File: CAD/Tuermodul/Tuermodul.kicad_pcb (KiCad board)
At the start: 2 copper layers, 202.2 x 100.1 mm, 136 parts, among them J101 Conn_02x16_Counter_Clockwise, J201 Conn_02x20_Counter_Clockwise, J301 Conn_02x20_Counter_Clockwise, Q205 Q_NPN_CBE, Q206 Q_NPN_CBE, Q207 Q_NPN_CBE, Q208 Q_NPN_CBE, Q209 Q_PMOS_GDS, Q210 Q_PMOS_GDS, Q211 Q_PMOS_GDS, Q212 Q_PMOS_GDS, Q213 Q_NPN_CBE, Q214 Q_NPN_CBE, Q215 Q_NPN_CBE, Q216 Q_NPN_CBE, Q301 Q_NPN_CBE, SW301 SW_SPDT_MSM, SW302 SW_SPDT_MSM, SW303 SW_SPDT_MSM, SW304 SW_SPDT_MSM, U101 93LC46B, U102 74HC595, U103 FT4232H, U104 MCP1825S, Y101 12MHz

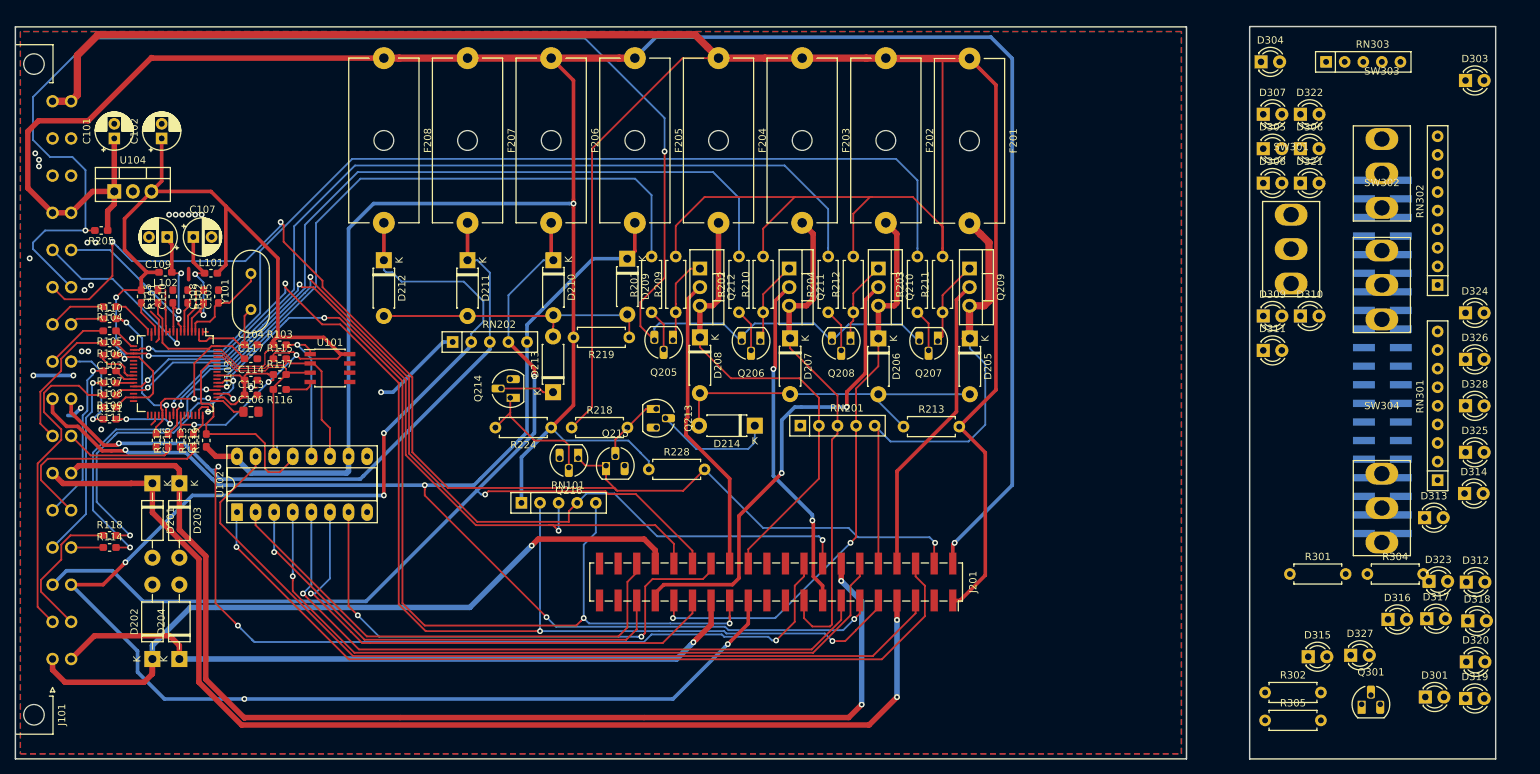
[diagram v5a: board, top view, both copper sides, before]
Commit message: -mod: Umbelegung Stecker zwischen Haupt und Frontplatine -add: 100n caps für MK Entprellung -mod: Routing Stecker -mod: Platzierung Front nach Vorgabe
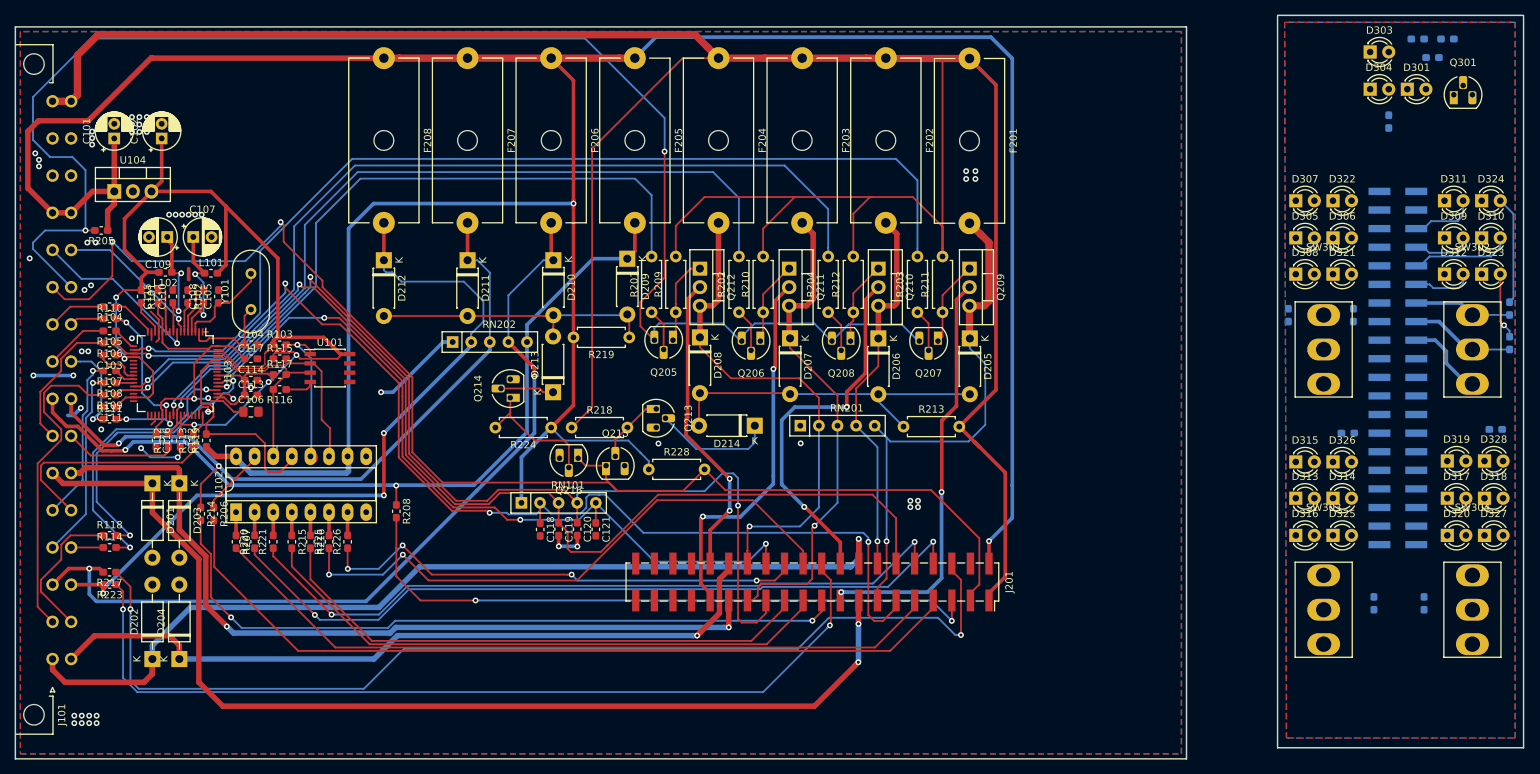
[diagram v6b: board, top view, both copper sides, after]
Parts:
- removed RN301: 8x2k7, Resistor_THT:R_Array_SIP9
- removed RN302: 8x10k, Resistor_THT:R_Array_SIP9
- removed RN303: 4x2k7, Resistor_THT:R_Array_SIP5
- added C118: 100n, Capacitor_SMD:C_0603_1608Metric_Pad1.05x0.95mm_HandSolder, F.Cu at (136.5, 113.1)
- added C119: 100n, Capacitor_SMD:C_0603_1608Metric_Pad1.05x0.95mm_HandSolder, F.Cu at (139.0, 113.1)
- added C120: 100n, Capacitor_SMD:C_0603_1608Metric_Pad1.05x0.95mm_HandSolder, F.Cu at (141.5, 113.1)
- added C121: 100n, Capacitor_SMD:C_0603_1608Metric_Pad1.05x0.95mm_HandSolder, F.Cu at (144.1, 113.1)
- added R206: 1k, Resistor_SMD:R_0603_1608Metric_Pad1.05x0.95mm_HandSolder, F.Cu at (91.9, 111.0)
- added R207: 1k, Resistor_SMD:R_0603_1608Metric_Pad1.05x0.95mm_HandSolder, F.Cu at (94.9, 114.8)
- added R208: 1k, Resistor_SMD:R_0603_1608Metric_Pad1.05x0.95mm_HandSolder, F.Cu at (116.8, 110.6)
- added R214: 1k, Resistor_SMD:R_0603_1608Metric_Pad1.05x0.95mm_HandSolder, F.Cu at (90.1, 111.0)
- added R215: 1k, Resistor_SMD:R_0603_1608Metric_Pad1.05x0.95mm_HandSolder, F.Cu at (102.5, 114.8)
- added R216: 1k, Resistor_SMD:R_0603_1608Metric_Pad1.05x0.95mm_HandSolder, F.Cu at (105.1, 114.8)
- added R217: 1k, Resistor_SMD:R_0603_1608Metric_Pad1.05x0.95mm_HandSolder, F.Cu at (77.6, 118.9)
- added R220: 1k, Resistor_SMD:R_0603_1608Metric_Pad1.05x0.95mm_HandSolder, F.Cu at (97.5, 114.8)
- added R221: 1k, Resistor_SMD:R_0603_1608Metric_Pad1.05x0.95mm_HandSolder, F.Cu at (100.0, 114.8)
- added R223: 1k, Resistor_SMD:R_0603_1608Metric_Pad1.05x0.95mm_HandSolder, F.Cu at (77.7, 120.6)
- added R225: 1k, Resistor_SMD:R_0603_1608Metric_Pad1.05x0.95mm_HandSolder, F.Cu at (107.6, 114.8)
- added R226: 1k, Resistor_SMD:R_0603_1608Metric_Pad1.05x0.95mm_HandSolder, F.Cu at (110.2, 114.8)
- added R303: 330R, Resistor_SMD:R_0603_1608Metric_Pad1.05x0.95mm_HandSolder, B.Cu at (256.4, 46.1)
- added R306: 4k7, Resistor_SMD:R_0603_1608Metric_Pad1.05x0.95mm_HandSolder, B.Cu at (238.7, 83.8)
- added R307: 4k7, Resistor_SMD:R_0603_1608Metric_Pad1.05x0.95mm_HandSolder, B.Cu at (268.9, 87.6)
- added R308: 4k7, Resistor_SMD:R_0603_1608Metric_Pad1.05x0.95mm_HandSolder, B.Cu at (268.9, 82.9)
- added R309: 4k7, Resistor_SMD:R_0603_1608Metric_Pad1.05x0.95mm_HandSolder, B.Cu at (250.4, 123.2)
- added R310: 4k7, Resistor_SMD:R_0603_1608Metric_Pad1.05x0.95mm_HandSolder, B.Cu at (246.8, 100.0)
- added R311: 4k7, Resistor_SMD:R_0603_1608Metric_Pad1.05x0.95mm_HandSolder, B.Cu at (257.2, 123.2)
- added R312: 4k7, Resistor_SMD:R_0603_1608Metric_Pad1.05x0.95mm_HandSolder, B.Cu at (267.0, 99.4)
- J201: value Conn_02x20_Counter_Clockwise -> Conn_02x20_Odd_Even
- R301, R302: footprint Resistor_THT:R_Axial_DIN0207_L6.3mm_D2.5mm_P7.62mm_Horizontal -> Resistor_SMD:R_0603_1608Metric_Pad1.05x0.95mm_HandSolder; moved to B.Cu
- R304: value 330R -> 1k; footprint Resistor_THT:R_Axial_DIN0207_L6.3mm_D2.5mm_P7.62mm_Horizontal -> Resistor_SMD:R_0603_1608Metric_Pad1.05x0.95mm_HandSolder; moved to B.Cu
- R305: value 1k -> 4k7; footprint Resistor_THT:R_Axial_DIN0207_L6.3mm_D2.5mm_P7.62mm_Horizontal -> Resistor_SMD:R_0603_1608Metric_Pad1.05x0.95mm_HandSolder; moved to B.Cu
- moved R302 89.7 mm to (258.4, 48.6)
- moved Q301 84.2 mm to (261.3, 53.7)
- moved D301 83.1 mm to (254.9, 53.0)
- moved R301 76.2 mm to (260.4, 46.1)
- moved R304 61.9 mm to (252.4, 57.4), turned to 270 degrees
- moved SW303 60.1 mm to (243.5, 124.1)
- moved R305 56.7 mm to (247.6, 83.8), turned to 270 degrees
- moved D323 42.6 mm to (265.1, 78.2)
- moved D312 42.2 mm to (260.0, 78.2)
- moved D319 32.5 mm to (260.4, 103.8)
- moved D311 32.1 mm to (260.0, 68.2)
- moved D310 27.0 mm to (265.1, 73.3)
- moved D309 27.0 mm to (260.0, 73.3)
- moved D315 26.7 mm to (239.7, 103.9)
- moved D327 24.5 mm to (265.5, 113.9)
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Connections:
- D305 pad 1: Net-(D305-Pad1) -> GNDA
- D306 pad 1: Net-(D306-Pad1) -> GNDA
- D307 pad 1: Net-(D307-Pad1) -> GNDA
- D309 pad 1: Net-(D309-Pad1) -> GNDA
- D310 pad 1: Net-(D310-Pad1) -> GNDA
- D311 pad 1: Net-(D311-Pad1) -> GNDA
- D313 pad 1: Net-(D313-Pad1) -> GNDA
- D314 pad 1: Net-(D314-Pad1) -> GNDA
- D315 pad 1: Net-(D315-Pad1) -> GNDA
- D317 pad 1: Net-(D317-Pad1) -> GNDA
- D318 pad 1: Net-(D318-Pad1) -> GNDA
- D319 pad 1: Net-(D319-Pad1) -> GNDA
- D321 pad 1: Net-(D321-Pad1) -> GNDA
- D321 pad 2: /Front/DoorA_Lock -> Net-(D321-Pad2)
- D322 pad 1: Net-(D322-Pad1) -> GNDA
- D322 pad 2: /Front/DoorA_12V -> Net-(D322-Pad2)
- D323 pad 1: Net-(D323-Pad1) -> GNDA
- D323 pad 2: /Front/DoorB_Lock -> Net-(D323-Pad2)
- D324 pad 1: Net-(D324-Pad1) -> GNDA
- D324 pad 2: /Front/DoorB_12V -> Net-(D324-Pad2)
- D325 pad 1: Net-(D325-Pad1) -> GNDA
- D325 pad 2: /Front/DoorC_Lock -> Net-(D325-Pad2)
- D326 pad 1: Net-(D326-Pad1) -> GNDA
- D326 pad 2: /Front/DoorC_12V -> Net-(D326-Pad2)
- D327 pad 1: Net-(D327-Pad1) -> GNDA
- D327 pad 2: /Front/DoorD_Lock -> Net-(D327-Pad2)
- D328 pad 1: Net-(D328-Pad1) -> GNDA
- D328 pad 2: /Front/DoorD_12V -> Net-(D328-Pad2)
- J201 pad 10: /Peripherie/DoorA_12V -> Net-(J201-Pad10)
- J201 pad 11: /DoorA_VCC -> /DoorA_MK
- J201 pad 12: /DC_Tx -> /DoorB_MK
- J201 pad 13: /DC_Rx -> /Peripherie/DoorA_12V
- J201 pad 14: /DoorC_Lock -> /Peripherie/DoorB_12V
- J201 pad 15: /Peripherie/DoorC_Auto -> /DoorA_Lock
- J201 pad 16: /DoorC_MK -> /DoorB_Lock
- J201 pad 17: /Peripherie/DoorC_12V -> /Peripherie/DoorA_Auto
- J201 pad 18: /DoorC_VCC -> /Peripherie/DoorB_Auto
- J201 pad 19: (no net) -> Net-(J201-Pad19)
- J201 pad 20: (no net) -> Net-(J201-Pad20)
- J201 pad 21: (no net) -> Net-(J201-Pad21)
- J201 pad 22: (no net) -> Net-(J201-Pad22)
- J201 pad 23: /DoorD_VCC -> Net-(J201-Pad23)
- J201 pad 24: /Peripherie/DoorD_12V -> Net-(J201-Pad24)
- J201 pad 25: /DoorD_MK -> /DoorC_MK
- J201 pad 26: /Peripherie/DoorD_Auto -> /DoorD_MK
- J201 pad 27: /DoorD_Lock -> /Peripherie/DoorC_12V
- J201 pad 28: /DD_Rx -> /Peripherie/DoorD_12V
- J201 pad 29: /DD_Tx -> /DoorC_Lock
- J201 pad 3: GND -> /Error
- J201 pad 30: /DoorB_VCC -> /DoorD_Lock
- J201 pad 31: /Peripherie/DoorB_12V -> /Peripherie/DoorC_Auto
- J201 pad 32: /DoorB_MK -> /Peripherie/DoorD_Auto
- J201 pad 33: /Peripherie/DoorB_Auto -> GND
- J201 pad 34: /DoorB_Lock -> GND
- J201 pad 35: /DB_Rx -> GND
- J201 pad 36: /DB_Tx -> GND
- J201 pad 37: (no net) -> GND
- J201 pad 38: (no net) -> GND
- J201 pad 39: (no net) -> GND
- J201 pad 4: /Error -> GND
- J201 pad 40: (no net) -> GND
- J201 pad 5: /DA_Tx -> Net-(J201-Pad5)
- J201 pad 6: /DA_Rx -> Net-(J201-Pad6)
- J201 pad 7: /DoorA_Lock -> Net-(J201-Pad7)
- J201 pad 8: /Peripherie/DoorA_Auto -> Net-(J201-Pad8)
- J201 pad 9: /DoorA_MK -> Net-(J201-Pad9)
- J301 pad 10: /Front/DoorA_12V -> /Front/DB_Rx
- J301 pad 11: /Front/DoorA_VCC -> /Front/DoorA_MK
- J301 pad 12: /Front/DC_Tx -> /Front/DoorB_MK
- J301 pad 13: /Front/DC_Rx -> /Front/DoorA_12V
- J301 pad 14: /Front/DoorC_Lock -> /Front/DoorB_12V
- J301 pad 15: /Front/DoorC_Auto -> /Front/DoorA_Lock
- J301 pad 16: /Front/DoorC_MK -> /Front/DoorB_Lock
- J301 pad 17: /Front/DoorC_12V -> /Front/DoorA_Auto
- J301 pad 18: /Front/DoorC_VCC -> /Front/DoorB_Auto
- J301 pad 19: (no net) -> /Front/DoorC_VCC
- J301 pad 20: (no net) -> /Front/DoorD_VCC
- J301 pad 21: (no net) -> /Front/DC_Tx
- J301 pad 22: (no net) -> /Front/DD_Tx
- J301 pad 23: /Front/DoorD_VCC -> /Front/DC_Rx
- J301 pad 24: /Front/DoorD_12V -> /Front/DD_Rx
- J301 pad 25: /Front/DoorD_MK -> /Front/DoorC_MK
- J301 pad 26: /Front/DoorD_Auto -> /Front/DoorD_MK
- J301 pad 27: /Front/DoorD_Lock -> /Front/DoorC_12V
- J301 pad 28: /Front/DD_Rx -> /Front/DoorD_12V
- J301 pad 29: /Front/DD_Tx -> /Front/DoorC_Lock
- J301 pad 3: GNDA -> /Front/Fuse_Error
- J301 pad 30: /Front/DoorB_VCC -> /Front/DoorD_Lock
- J301 pad 31: /Front/DoorB_12V -> /Front/DoorC_Auto
- J301 pad 32: /Front/DoorB_MK -> /Front/DoorD_Auto
- J301 pad 33: /Front/DoorB_Auto -> GNDA
- J301 pad 34: /Front/DoorB_Lock -> GNDA
- J301 pad 35: /Front/DB_Rx -> GNDA
- J301 pad 36: /Front/DB_Tx -> GNDA
- J301 pad 37: (no net) -> GNDA
- J301 pad 38: (no net) -> GNDA
- J301 pad 39: (no net) -> GNDA
- J301 pad 4: /Front/Fuse_Error -> GNDA
- J301 pad 40: (no net) -> GNDA
- J301 pad 5: /Front/DA_Tx -> /Front/DoorA_VCC
- J301 pad 6: /Front/DA_Rx -> /Front/DoorB_VCC
- J301 pad 7: /Front/DoorA_Lock -> /Front/DA_Tx
- J301 pad 8: /Front/DoorA_Auto -> /Front/DB_Tx
- J301 pad 9: /Front/DoorA_MK -> /Front/DA_Rx
- R304 pad 1: +5P -> +12P
- R304 pad 2: Net-(D303-Pad2) -> Net-(D304-Pad2)
- R305 pad 1: +12P -> Net-(D321-Pad2)
- R305 pad 2: Net-(D304-Pad2) -> /Front/DoorA_Lock
- U101 pad 6: (no net) -> Net-(U101-Pad6)
- U101 pad 7: (no net) -> Net-(U101-Pad7)
- U102 pad 9: (no net) -> Net-(U102-Pad9)
- U103 pad 21: (no net) -> Net-(U103-Pad21)
- U103 pad 22: (no net) -> Net-(U103-Pad22)
- U103 pad 23: (no net) -> Net-(U103-Pad23)
- U103 pad 24: (no net) -> Net-(U103-Pad24)
- U103 pad 30: (no net) -> Net-(U103-Pad30)
- U103 pad 32: (no net) -> Net-(U103-Pad32)
- U103 pad 33: (no net) -> Net-(U103-Pad33)
- U103 pad 34: (no net) -> Net-(U103-Pad34)
- U103 pad 36: (no net) -> Net-(U103-Pad36)
- U103 pad 43: (no net) -> Net-(U103-Pad43)
- U103 pad 44: (no net) -> Net-(U103-Pad44)
- U103 pad 45: (no net) -> Net-(U103-Pad45)
- U103 pad 46: (no net) -> Net-(U103-Pad46)
- U103 pad 55: (no net) -> Net-(U103-Pad55)
- U103 pad 57: (no net) -> Net-(U103-Pad57)
- U103 pad 58: (no net) -> Net-(U103-Pad58)
- U103 pad 59: (no net) -> Net-(U103-Pad59)
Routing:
- net Net-(J201-Pad6): track 0.00 -> 144.8 mm, vias 0 -> 2
- net Net-(J201-Pad20): track 0.00 -> 123.3 mm, vias 0 -> 2
- net Net-(J201-Pad7): track 0.00 -> 113.9 mm
- net /DA_Rx: track 115.4 -> 3.17 mm, vias 1 -> 0
- net /DA_Tx: track 117.8 -> 9.30 mm
- net /DoorD_VCC: track 209.8 -> 103.8 mm, vias 5 -> 3
- net /DoorC_VCC: track 202.4 -> 97.3 mm, vias 4 -> 2
- net Net-(J201-Pad8): track 0.00 -> 104.7 mm, vias 0 -> 2
- net Net-(J201-Pad9): track 0.00 -> 101.6 mm
- net Net-(J201-Pad19): track 0.00 -> 99.7 mm, vias 0 -> 2
- net Net-(J201-Pad10): track 0.00 -> 99.1 mm, vias 0 -> 2
- net /DC_Tx: track 100.2 -> 3.17 mm, vias 1 -> 0
- net /DC_Rx: track 92.6 -> 3.17 mm, vias 1 -> 0
- net Net-(J201-Pad5): track 0.00 -> 89.3 mm, vias 0 -> 2
- net Net-(J201-Pad22): track 0.00 -> 80.1 mm, vias 0 -> 2
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- added copper zone on B.Cu, net GNDA
- added copper zone on F.Cu, net GNDA
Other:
- board size 202.2 x 100.1 mm -> 206.1 x 101.6 mm

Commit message: -mod: layout update from 10.03.19
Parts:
- added REF**: MountingHole_2.5mm, MountingHole:MountingHole_2.5mm, F.Cu at (253.7, 60.6)
- added REF**: MountingHole_2.5mm, MountingHole:MountingHole_2.5mm, F.Cu at (253.7, 136.8)
- moved R305 9.67 mm to (238.7, 87.6)
- moved R304 5.51 mm to (246.9, 56.8), turned to 0 degrees
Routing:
- net /Front/DoorD_12V: track 0.00 -> 39.6 mm, vias 0 -> 3
- net /Front/DoorD_Lock: track 0.00 -> 37.0 mm, vias 0 -> 1
- net /Front/DoorC_Lock: track 0.00 -> 36.4 mm, vias 0 -> 1
- net /Front/DoorC_12V: track 0.00 -> 33.0 mm, vias 0 -> 1
- net /Front/DoorC_Auto: track 0.00 -> 32.0 mm, vias 0 -> 1
- net /Front/DoorD_Auto: track 0.00 -> 29.7 mm, vias 0 -> 1
- net Net-(D322-Pad2): track 0.00 -> 28.1 mm
- net +5P: track 0.00 -> 26.8 mm, vias 0 -> 2
- net /Front/DC_Tx: track 0.00 -> 25.5 mm, vias 0 -> 1
- net /Front/DD_Rx: track 0.00 -> 25.5 mm, vias 0 -> 1
- net /Front/DoorC_MK: track 0.00 -> 24.7 mm, vias 0 -> 1
- net /Front/DD_Tx: track 0.00 -> 22.7 mm, vias 0 -> 2
- net /Front/DoorD_MK: track 0.00 -> 21.6 mm, vias 0 -> 1
- net /Front/Fuse_Error: track 0.00 -> 21.6 mm
- net /Front/DC_Rx: track 0.00 -> 18.7 mm, vias 0 -> 1
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
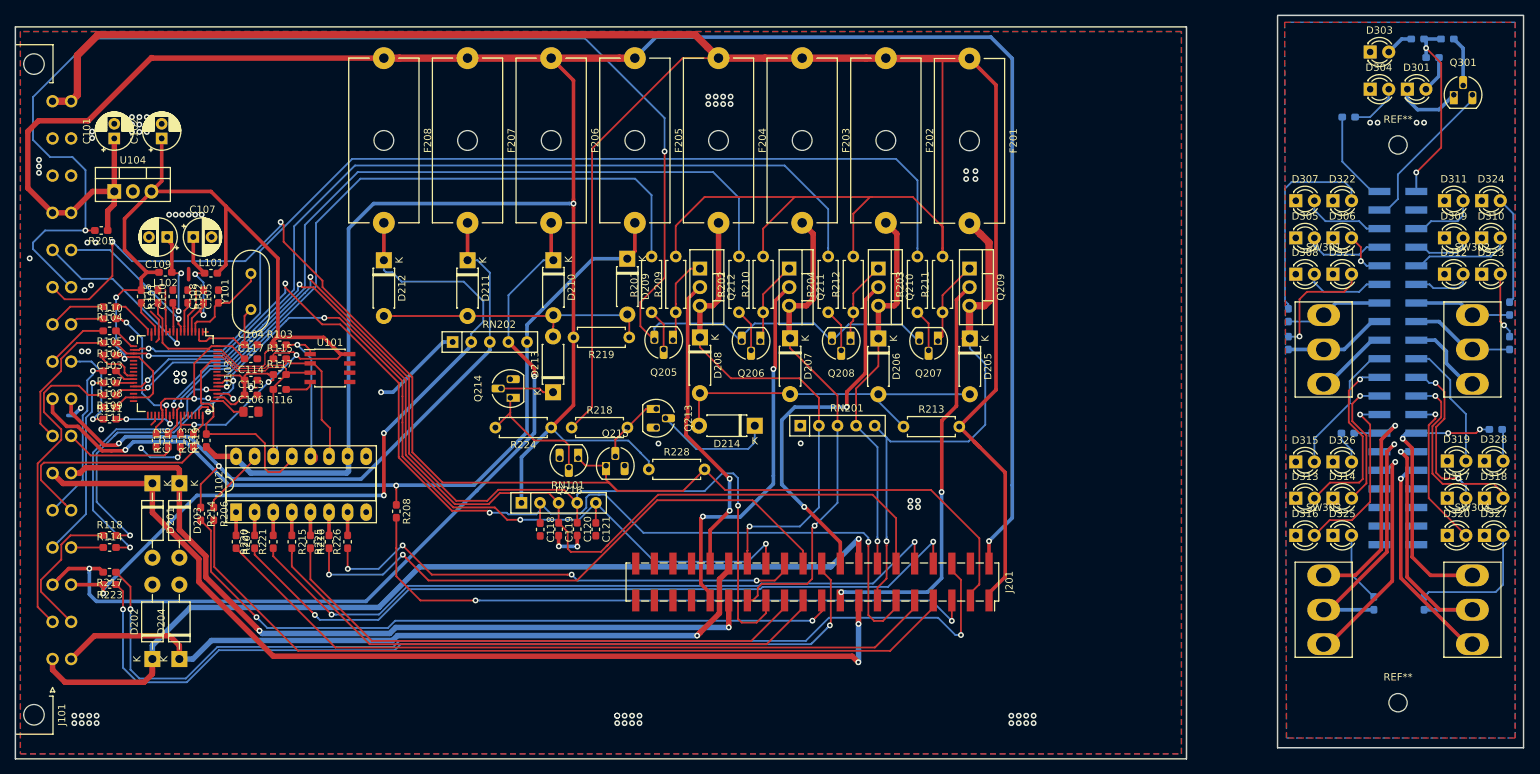
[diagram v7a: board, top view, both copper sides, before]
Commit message: -mod: Änderungen aus Review in Schaltplan und Layout
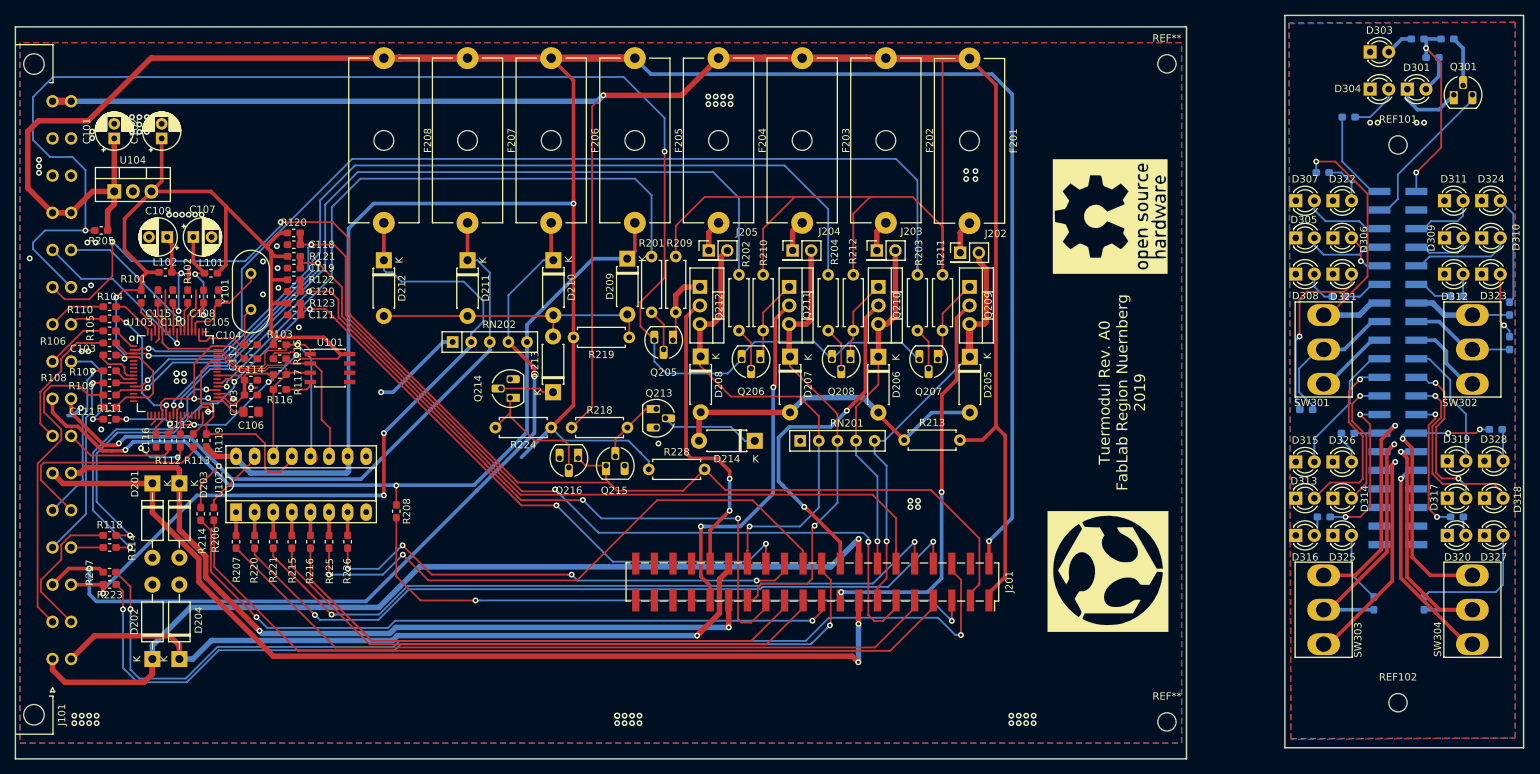
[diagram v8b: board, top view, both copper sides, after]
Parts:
- removed RN101: 2k7, Resistor_THT:R_Array_SIP5
- added G101: LOGO, FLN_logo:fln_logo, F.Cu at (214.0, 118.9)
- added G102: LOGO, OSH_logo:OSH_logo, F.Cu at (214.3, 70.4)
- added J202: Conn_02x01, Connector_PinHeader_2.54mm:PinHeader_2x01_P2.54mm_Vertical, F.Cu at (193.9, 75.3)
- added J203: Conn_02x01, Connector_PinHeader_2.54mm:PinHeader_2x01_P2.54mm_Vertical, F.Cu at (182.5, 75.0)
- added J204: Conn_02x01, Connector_PinHeader_2.54mm:PinHeader_2x01_P2.54mm_Vertical, F.Cu at (171.0, 75.0)
- added J205: Conn_02x01, Connector_PinHeader_2.54mm:PinHeader_2x01_P2.54mm_Vertical, F.Cu at (159.5, 75.0)
- added R120: 1k, Resistor_SMD:R_0603_1608Metric_Pad1.05x0.95mm_HandSolder, F.Cu at (102.8, 72.6)
- added R121: 1k, Resistor_SMD:R_0603_1608Metric_Pad1.05x0.95mm_HandSolder, F.Cu at (102.8, 75.8)
- added R122: 1k, Resistor_SMD:R_0603_1608Metric_Pad1.05x0.95mm_HandSolder, F.Cu at (102.8, 79.0)
- added R123: 1k, Resistor_SMD:R_0603_1608Metric_Pad1.05x0.95mm_HandSolder, F.Cu at (102.8, 82.2)
- added R313: 470R, Resistor_SMD:R_0603_1608Metric_Pad1.05x0.95mm_HandSolder, B.Cu at (245.6, 81.3)
- added R314: 470R, Resistor_SMD:R_0603_1608Metric_Pad1.05x0.95mm_HandSolder, B.Cu at (261.7, 81.2)
- added R315: 470R, Resistor_SMD:R_0603_1608Metric_Pad1.05x0.95mm_HandSolder, B.Cu at (243.5, 111.4)
- added R316: 470R, Resistor_SMD:R_0603_1608Metric_Pad1.05x0.95mm_HandSolder, B.Cu at (261.7, 111.4)
- added REF**: MountingHole_2.5mm, MountingHole:MountingHole_2.5mm, F.Cu at (222.1, 49.5)
- added REF**: MountingHole_2.5mm, MountingHole:MountingHole_2.5mm, F.Cu at (222.1, 139.4)
- R106, R109, R112, R118: value 33R -> 100R
- moved C118 51.4 mm to (102.8, 74.2), turned to 180 degrees
- moved C119 50.8 mm to (102.8, 77.4), turned to 180 degrees
- moved C121 50.5 mm to (102.9, 83.8), turned to 180 degrees
- moved C120 50.5 mm to (102.8, 80.6), turned to 180 degrees
- moved R306 20.0 mm to (243.4, 64.3), turned to 180 degrees
- moved R305 9.43 mm to (241.1, 96.8), turned to 0 degrees
- moved D208 2.61 mm to (158.4, 89.5)
- moved D205 2.50 mm to (195.2, 89.5)
- moved D206 2.50 mm to (182.7, 89.5)
- moved D207 2.50 mm to (170.6, 89.5)
- moved Q206 2.50 mm to (166.5, 89.9)
- moved Q207 2.50 mm to (190.8, 89.9)
- moved Q208 2.50 mm to (178.9, 89.9)
- moved Q209 2.50 mm to (195.1, 80.0)
- moved Q210 2.50 mm to (182.7, 80.0)
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- renumbered REF** to REF101, REF** to REF102
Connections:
- D308 pad 2: /Front/DoorA_MK -> Net-(D308-Pad2)
- D312 pad 2: /Front/DoorB_MK -> Net-(D312-Pad2)
- D316 pad 2: /Front/DoorC_MK -> Net-(D316-Pad2)
- D320 pad 2: /Front/DoorD_MK -> Net-(D320-Pad2)
- F201 pad 2: /Peripherie/DoorA_12V -> Net-(F201-Pad2)
- F202 pad 2: /Peripherie/DoorB_12V -> Net-(F202-Pad2)
- F203 pad 2: /Peripherie/DoorC_12V -> Net-(F203-Pad2)
- F204 pad 2: /Peripherie/DoorD_12V -> Net-(F204-Pad2)
- U101 pad 6: Net-(U101-Pad6) -> (no net)
- U101 pad 7: Net-(U101-Pad7) -> (no net)
- U102 pad 9: Net-(U102-Pad9) -> (no net)
- U103 pad 21: Net-(U103-Pad21) -> (no net)
- U103 pad 22: Net-(U103-Pad22) -> (no net)
- U103 pad 23: Net-(U103-Pad23) -> (no net)
- U103 pad 24: Net-(U103-Pad24) -> (no net)
- U103 pad 30: Net-(U103-Pad30) -> (no net)
- U103 pad 32: Net-(U103-Pad32) -> (no net)
- U103 pad 33: Net-(U103-Pad33) -> (no net)
- U103 pad 34: Net-(U103-Pad34) -> (no net)
- U103 pad 36: Net-(U103-Pad36) -> (no net)
- U103 pad 43: Net-(U103-Pad43) -> (no net)
- U103 pad 44: Net-(U103-Pad44) -> (no net)
- U103 pad 45: Net-(U103-Pad45) -> (no net)
- U103 pad 46: Net-(U103-Pad46) -> (no net)
- U103 pad 55: Net-(U103-Pad55) -> (no net)
- U103 pad 57: Net-(U103-Pad57) -> (no net)
- U103 pad 58: Net-(U103-Pad58) -> (no net)
- U103 pad 59: Net-(U103-Pad59) -> (no net)
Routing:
- net /Front/DoorA_12V: track 13.5 -> 39.4 mm, vias 0 -> 1
- net Net-(D322-Pad2): track 28.1 -> 6.11 mm
- net /DoorC_MK: track 141.8 -> 124.7 mm, vias 3 -> 4
- net /Peripherie/DoorA_12V: track 74.6 -> 58.5 mm
- net +12V: track 373.0 -> 359.8 mm, vias 0 -> 1
- net +5V: track 415.6 -> 404.2 mm
- net +3V3: track 159.3 -> 170.2 mm
- net Net-(D321-Pad2): track 16.2 -> 25.2 mm
- net /DoorB_MK: track 149.6 -> 141.6 mm
- net /DoorD_MK: track 146.4 -> 140.0 mm
- net /Front/DoorA_Lock: track 14.0 -> 20.0 mm
- net /Front/DoorA_MK: track 11.0 -> 5.37 mm
- net GND: track 64.0 -> 58.5 mm, vias 88 -> 91
- net Net-(D308-Pad2): track 0.00 -> 4.73 mm
- net Net-(F201-Pad2): track 0.00 -> 4.55 mm
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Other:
- outline, holes or cut-outs redrawn
- board text added: "Tuermodul Rev. A0 FabLab Region Nuernberg 2019"
